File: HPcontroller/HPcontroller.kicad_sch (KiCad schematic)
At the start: 34 parts, among them J1 Screw_Terminal_01x02, Q1 Q_Dual_NMOS_S1G1S2G2D2D2D1D1, U1 Adafruit_QTPY_ESP32-C3, U2 NCP81071B, U4 VR10S3V3, U5 ER-OLED0.49-1_MODULE, U6 Adafruit_MAX31850

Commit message: fixed minor issues, added mounting
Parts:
- added H1: (no value), symbol Mechanical:MountingHole
- added H2, H3, H4: MountingHole, symbol Mechanical:MountingHole
- J1: footprint (none) -> connector_custom:PD_trigger
- R11: footprint (none) -> connector_custom:AMASS_XT60PW-M
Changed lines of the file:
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@@
+    (stroke (width 0) (type default) (color 0 0 0 0))
+  )
+  (polyline (pts (xy 149.86 191.77) (xy 15.24 191.77))
     (stroke (width 0) (type default) (color 0 0 0 0))
   )
@@
     (stroke (width 0) (type default) (color 0 0 0 0))
   )
+  (polyline (pts (xy 149.86 166.37) (xy 149.86 191.77))
+    (stroke (width 0) (type default) (color 0 0 0 0))
+  )
   (wire (pts (xy 19.05 95.25) (xy 19.05 97.79))
     (stroke (width 0) (type default) (color 0 0 0 0))
@@
     (stroke (width 0) (type default) (color 0 0 0 0))
   )
+  (polyline (pts (xy 15.24 166.37) (xy 15.24 191.77))
+    (stroke (width 0) (type default) (color 0 0 0 0))
+  )
   (wire (pts (xy 19.05 105.41) (xy 19.05 107.95))
     (stroke (width 0) (type default) (color 0 0 0 0))
@@
   )
   (wire (pts (xy 205.74 118.11) (xy 198.12 118.11))
+    (stroke (width 0) (type default) (color 0 0 0 0))
+  )
+  (polyline (pts (xy 15.24 166.37) (xy 149.86 166.37))
     (stroke (width 0) (type default) (color 0 0 0 0))
   )
@@
     (pin "1")
     (pin "2")
+  )
+  (symbol (lib_id "Mechanical:MountingHole") (at 38.1 182.88 0) (unit 1)
+    (in_bom yes) (on_board yes) (fields_autoplaced)
+    (property "Reference" "H2" (id 0) (at 40.64 182.0453 0)
+      (effects (font (size 1.27 1.27)) (justify left))
+    )
+    (property "Value" "MountingHole" (id 1) (at 40.64 184.5822 0)
+      (effects (font (size 1.27 1.27)) (justify left))
+    )
+    (property "Footprint" "" (id 2) (at 38.1 182.88 0)
+      (effects (font (size 1.27 1.27)) hide)
+    )
+    (property "Datasheet" "~" (id 3) (at 38.1 182.88 0)
+      (effects (font (size 1.27 1.27)) hide)
+    )
   )
   (symbol (lib_id "Device:R") (at 172.72 124.46 0) (unit 1)
@@
     (pin "2")
   )
+  (symbol (lib_id "Mechanical:MountingHole") (at 38.1 176.53 0) (unit 1)
+    (in_bom yes) (on_board yes) (fields_autoplaced)
+    (property "Reference" "H1" (id 0) (at 40.64 175.6953 0)
+      (effects (font (size 1.27 1.27)) (justify left))
+    )
+    (property "Value" "" (id 1) (at 40.64 178.2322 0)
+      (effects (font (size 1.27 1.27)) (justify left))
+    )
+    (property "Footprint" "" (id 2) (at 38.1 176.53 0)
+      (effects (font (size 1.27 1.27)) hide)
+    )
+    (property "Datasheet" "~" (id 3) (at 38.1 176.53 0)
+      (effects (font (size 1.27 1.27)) hide)
+    )
+  )
   (symbol (lib_id "dcdcmodule:VR10S3V3") (at 102.87 33.655 0) (unit 1)
     (in_bom yes) (on_board yes) (fields_autoplaced)
@@
       (effects (font (size 1.27 1.27)) (justify right))
     )
-    (property "Footprint" "" (id 2) (at 66.04 35.56 0)
+    (property "Footprint" "connector_custom:PD_trigger" (id 2) (at 66.04 35.56 0)
       (effects (font (size 1.27 1.27)) hide)
     )
@@
     (pin "2")
   )
+  (symbol (lib_id "Mechanical:MountingHole") (at 55.88 182.88 0) (unit 1)
+    (in_bom yes) (on_board yes) (fields_autoplaced)
+    (property "Reference" "H4" (id 0) (at 58.42 182.0453 0)
+      (effects (font (size 1.27 1.27)) (justify left))
+    )
+    (property "Value" "MountingHole" (id 1) (at 58.42 184.5822 0)
+      (effects (font (size 1.27 1.27)) (justify left))
+    )
+    (property "Footprint" "" (id 2) (at 55.88 182.88 0)
+      (effects (font (size 1.27 1.27)) hide)
+    )
+    (property "Datasheet" "~" (id 3) (at 55.88 182.88 0)
+      (effects (font (size 1.27 1.27)) hide)
+    )
+  )
   (symbol (lib_id "power:+3V3") (at 36.83 95.25 0) (unit 1)
     (in_bom yes) (on_board yes) (fields_autoplaced)
@@
       (effects (font (size 1.27 1.27)) (justify right))
     )
-    (property "Footprint" "" (id 2) (at 249.428 91.44 90)
+    (property "Footprint" "connector_custom:AMASS_XT60PW-M" (id 2) (at 249.428 91.44 90)
       (effects (font (size 1.27 1.27)) hide)
     )
@@
     (pin "1")
     (pin "2")
+  )
+  (symbol (lib_id "Mechanical:MountingHole") (at 55.88 176.53 0) (unit 1)
+    (in_bom yes) (on_board yes) (fields_autoplaced)
+    (property "Reference" "H3" (id 0) (at 58.42 175.6953 0)
+      (effects (font (size 1.27 1.27)) (justify left))
+    )
+    (property "Value" "MountingHole" (id 1) (at 58.42 178.2322 0)
+      (effects (font (size 1.27 1.27)) (justify left))
+    )
+    (property "Footprint" "" (id 2) (at 55.88 176.53 0)
+      (effects (font (size 1.27 1.27)) hide)
+    )
+    (property "Datasheet" "~" (id 3) (at 55.88 176.53 0)
+      (effects (font (size 1.27 1.27)) hide)
+    )
   )
   (symbol (lib_id "Switch:SW_SPST") (at 163.83 90.17 0) (unit 1)
@@
       (reference "D_RUN1") (unit 1) (value "LED") (footprint "LED_SMD:LED_0603_1608Metric_Pad1.05x0.95mm_HandSolder")
     )
+    (path "/5d19829e-e95d-4ae6-bbd1-c9f884742daf"
+      (reference "H1") (unit 1) (value "MountingHole") (footprint "MountingHole:MountingHole_3.2mm_M3_ISO14580")
+    )
+    (path "/0dd8a88a-3c85-402b-a2dd-d98bc5ddbd5e"
+      (reference "H2") (unit 1) (value "MountingHole") (footprint "MountingHole:MountingHole_3.2mm_M3_ISO14580")
+    )
+    (path "/f6ed04a0-ba11-4b67-938a-2ac59d652fb6"
+      (reference "H3") (unit 1) (value "MountingHole") (footprint "MountingHole:MountingHole_3.2mm_M3_ISO14580")
+    )
+    (path "/d63d48bb-8353-4f86-81fa-3af96f4dae35"
+      (reference "H4") (unit 1) (value "MountingHole") (footprint "MountingHole:MountingHole_3.2mm_M3_ISO14580")
+    )
     (path "/717c5635-2c87-4cb5-ba9c-2320b08b52ea"

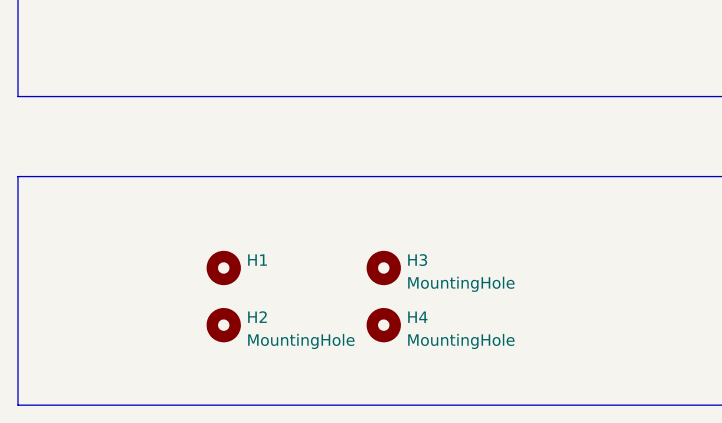
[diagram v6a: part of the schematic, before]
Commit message: added upllup to thermal protection circuit
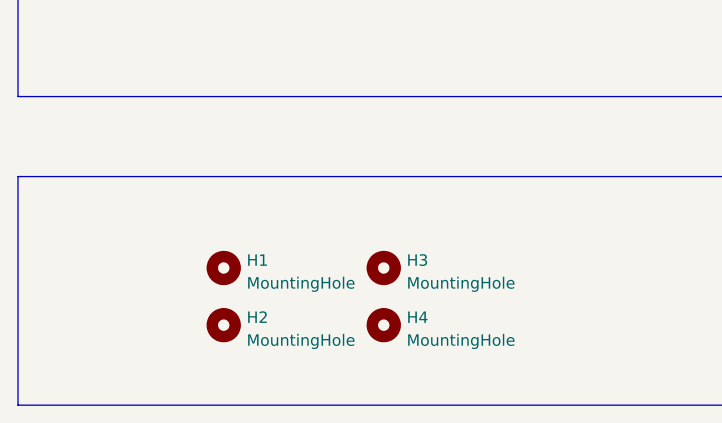
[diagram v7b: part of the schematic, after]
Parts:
- H1: value (none) -> MountingHole; footprint (none) -> MountingHole:MountingHole_3.2mm_M3_ISO14580
- H2, H3, H4: footprint (none) -> MountingHole:MountingHole_3.2mm_M3_ISO14580
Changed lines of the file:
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@@
       (effects (font (size 1.27 1.27)) (justify left))
     )
-    (property "Footprint" "" (id 2) (at 38.1 182.88 0)
+    (property "Footprint" "MountingHole:MountingHole_3.2mm_M3_ISO14580" (id 2) (at 38.1 182.88 0)
       (effects (font (size 1.27 1.27)) hide)
     )
@@
       (effects (font (size 1.27 1.27)) (justify left))
     )
-    (property "Value" "" (id 1) (at 40.64 178.2322 0)
-      (effects (font (size 1.27 1.27)) (justify left))
-    )
-    (property "Footprint" "" (id 2) (at 38.1 176.53 0)
+    (property "Value" "MountingHole" (id 1) (at 40.64 178.2322 0)
+      (effects (font (size 1.27 1.27)) (justify left))
+    )
+    (property "Footprint" "MountingHole:MountingHole_3.2mm_M3_ISO14580" (id 2) (at 38.1 176.53 0)
       (effects (font (size 1.27 1.27)) hide)
     )
@@
       (effects (font (size 1.27 1.27)) (justify left))
     )
-    (property "Footprint" "" (id 2) (at 55.88 182.88 0)
+    (property "Footprint" "MountingHole:MountingHole_3.2mm_M3_ISO14580" (id 2) (at 55.88 182.88 0)
       (effects (font (size 1.27 1.27)) hide)
     )
@@
       (effects (font (size 1.27 1.27)) (justify left))
     )
-    (property "Footprint" "" (id 2) (at 55.88 176.53 0)
+    (property "Footprint" "MountingHole:MountingHole_3.2mm_M3_ISO14580" (id 2) (at 55.88 176.53 0)
       (effects (font (size 1.27 1.27)) hide)
     )
@@
       (reference "R14") (unit 1) (value "4k7") (footprint "Resistor_SMD:R_0805_2012Metric_Pad1.20x1.40mm_HandSolder")
     )
+    (path "/2576b983-b407-4bb3-870d-6fa0fab97bf4/d7e2b224-b62c-427b-bb61-19f825a45bc1"
+      (reference "R15") (unit 1) (value "10k") (footprint "Resistor_SMD:R_0805_2012Metric_Pad1.20x1.40mm_HandSolder")
+    )
     (path "/2576b983-b407-4bb3-870d-6fa0fab97bf4/002ca803-9c32-4dcb-a365-3a6ffc3281e2"

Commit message: started revision
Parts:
- removed C2, C3: C, Capacitor_SMD:C_0805_2012Metric_Pad1.18x1.45mm_HandSolder, symbol Device:C
- removed J1: Screw_Terminal_01x02, connector_custom:PD_trigger, symbol Connector:Screw_Terminal_01x02
- removed U4: VR10S3V3, DevBoards:3pinDCDC, symbol dcdcmodule:VR10S3V3
- added U7: Adafruit_QTPY_ESP32-C3, DevBoards:QTPY ESP32 C3, symbol DevBoards:Adafruit_QTPY_ESP32-C3
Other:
- added sheet HEATER DRIVE (HeaterDrive.kicad_sch)
- added sheet USB POWER IN (usb_power_in.kicad_sch)
- note removed: "VCC should be 20V from USB PD"
- moved on the sheet: C1, C4, D1, D_3V3_POW1, D_HEAT1, D_HOT1, D_PD_POW1, D_RUN1, H1, H2, H3, H4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
